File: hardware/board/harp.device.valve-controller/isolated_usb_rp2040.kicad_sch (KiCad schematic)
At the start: 49 parts, among them J2 Conn_01x03_Male, J4 AudioJack3, J5 USB_C_Receptacle_USB2.0, U2 TPD2EUSB30, U3 ADUM4160, U4 RP2040, U5 W25Q16JVUXIQ, X1 ECS-TXO-2016

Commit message: route pcb
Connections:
- net EXT_TRIG0 renamed GPIO0
- net EXT_TRIG1 renamed GPIO1
- net EXT_TRIG2 renamed GPIO2
- net EXT_TRIG3 renamed GPIO3
- net POKE_IN0 renamed GPIO4
- net POKE_IN1 renamed GPIO5
- net POKE_IN2 renamed GPIO6
- net POKE_IN3 renamed GPIO7
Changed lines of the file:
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@@
 		)
 	)
-	(hierarchical_label "EXT_TRIG1"
+	(hierarchical_label "GPIO1"
 		(shape input)
 		(at 227.33 133.35 0)
@@
 		)
 	)
-	(hierarchical_label "POKE_IN0"
+	(hierarchical_label "GPIO4"
 		(shape input)
 		(at 227.33 143.51 0)
@@
 		)
 	)
-	(hierarchical_label "EXT_TRIG2"
+	(hierarchical_label "GPIO2"
 		(shape input)
 		(at 227.33 135.89 0)
@@
 		)
 	)
-	(hierarchical_label "POKE_IN1"
+	(hierarchical_label "GPIO5"
 		(shape input)
 		(at 227.33 146.05 0)
@@
 		)
 	)
-	(hierarchical_label "EXT_TRIG3"
+	(hierarchical_label "GPIO3"
 		(shape input)
 		(at 227.33 138.43 0)
@@
 		)
 	)
-	(hierarchical_label "POKE_IN2"
+	(hierarchical_label "GPIO6"
 		(shape input)
 		(at 227.33 148.59 0)
@@
 		)
 	)
-	(hierarchical_label "EXT_TRIG0"
+	(hierarchical_label "GPIO0"
 		(shape input)
 		(at 227.33 130.81 0)
@@
 		)
 	)
-	(hierarchical_label "POKE_IN3"
+	(hierarchical_label "GPIO7"
 		(shape input)
 		(at 227.33 151.13 0)

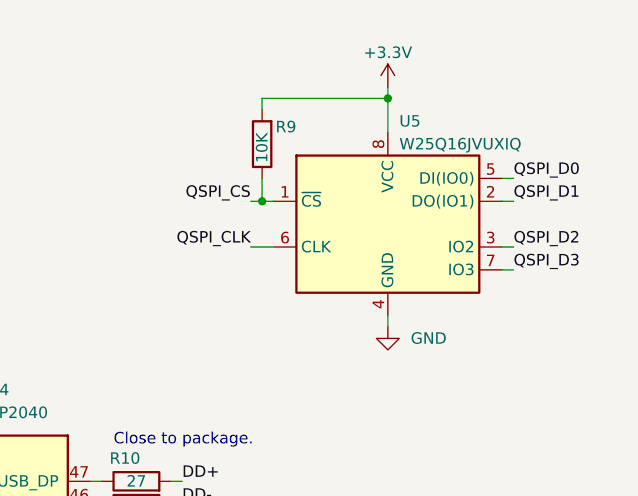
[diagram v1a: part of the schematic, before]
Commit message: update pcb power supply
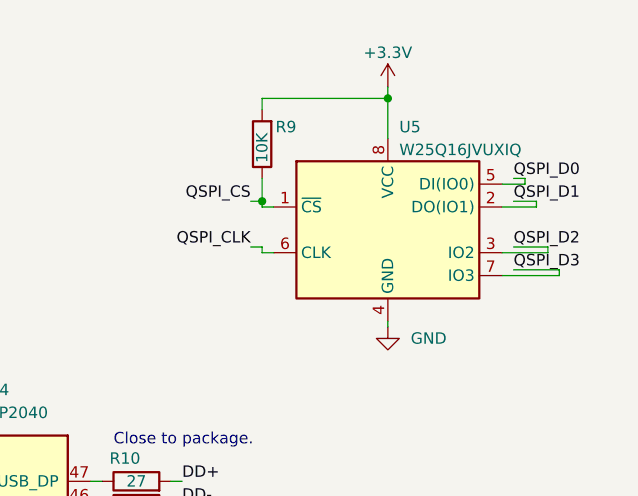
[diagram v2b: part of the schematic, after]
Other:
- moved on the sheet: U5
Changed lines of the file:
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@@
 	(wire
 		(pts
+			(xy 273.05 31.115) (xy 271.78 31.115)
+		)
+		(stroke
+			(width 0)
+			(type default)
+		)
+	)
+	(wire
+		(pts
 			(xy 106.68 27.94) (xy 106.68 31.75)
 		)
@@
 	(wire
 		(pts
-			(xy 257.81 22.225) (xy 257.81 26.035)
+			(xy 257.81 22.225) (xy 257.81 26.67)
 		)
 		(stroke
@@
 	(wire
 		(pts
-			(xy 270.51 38.735) (xy 271.78 38.735)
+			(xy 270.51 39.37) (xy 275.59 39.37)
 		)
 		(stroke
@@
 	(wire
 		(pts
+			(xy 275.59 39.37) (xy 275.59 38.735)
+		)
+		(stroke
+			(width 0)
+			(type default)
+		)
+	)
+	(wire
+		(pts
 			(xy 66.675 38.735) (xy 66.675 53.975)
 		)
@@
 	(wire
 		(pts
+			(xy 274.32 33.655) (xy 271.78 33.655)
+		)
+		(stroke
+			(width 0)
+			(type default)
+		)
+	)
+	(wire
+		(pts
 			(xy 242.57 33.655) (xy 243.84 33.655)
 		)
@@
 	(wire
 		(pts
+			(xy 275.59 38.735) (xy 271.78 38.735)
+		)
+		(stroke
+			(width 0)
+			(type default)
+		)
+	)
+	(wire
+		(pts
 			(xy 42.545 45.085) (xy 41.275 45.085)
 		)
@@
 	(wire
 		(pts
-			(xy 243.84 33.655) (xy 245.11 33.655)
+			(xy 243.84 34.29) (xy 245.11 34.29)
 		)
 		(stroke
@@
 	(wire
 		(pts
+			(xy 276.86 41.275) (xy 271.78 41.275)
+		)
+		(stroke
+			(width 0)
+			(type default)
+		)
+	)
+	(wire
+		(pts
 			(xy 70.485 18.415) (xy 70.485 19.685)
 		)
@@
 	(wire
 		(pts
+			(xy 276.86 41.91) (xy 276.86 41.275)
+		)
+		(stroke
+			(width 0)
+			(type default)
+		)
+	)
+	(wire
+		(pts
 			(xy 180.34 55.88) (xy 175.26 55.88)
 		)
@@
 	(wire
 		(pts
+			(xy 274.32 34.29) (xy 274.32 33.655)
+		)
+		(stroke
+			(width 0)
+			(type default)
+		)
+	)
+	(wire
+		(pts
 			(xy 50.8 180.975) (xy 50.8 179.705)
 		)
@@
 	(wire
 		(pts
-			(xy 257.81 46.355) (xy 257.81 47.625)
+			(xy 257.81 46.99) (xy 257.81 47.625)
 		)
 		(stroke
@@
 	(wire
 		(pts
+			(xy 273.05 31.75) (xy 273.05 31.115)
+		)
+		(stroke
+			(width 0)
+			(type default)
+		)
+	)
+	(wire
+		(pts
 			(xy 224.79 102.87) (xy 227.33 102.87)
 		)
@@
 	(wire
 		(pts
+			(xy 243.84 39.37) (xy 243.84 38.735)
+		)
+		(stroke
+			(width 0)
+			(type default)
+		)
+	)
+	(wire
+		(pts
 			(xy 118.11 22.86) (xy 118.11 26.67)
 		)
@@
 	(wire
 		(pts
+			(xy 243.84 38.735) (xy 242.57 38.735)
+		)
+		(stroke
+			(width 0)
+			(type default)
+		)
+	)
+	(wire
+		(pts
 			(xy 160.02 110.49) (xy 161.29 110.49)
 		)
@@
 	(wire
 		(pts
-			(xy 270.51 33.655) (xy 271.78 33.655)
+			(xy 270.51 34.29) (xy 274.32 34.29)
 		)
 		(stroke
@@
 	(wire
 		(pts
-			(xy 270.51 31.115) (xy 271.78 31.115)
+			(xy 270.51 31.75) (xy 273.05 31.75)
 		)
 		(stroke
@@
 	(wire
 		(pts
+			(xy 243.84 34.29) (xy 243.84 33.655)
+		)
+		(stroke
+			(width 0)
+			(type default)
+		)
+	)
+	(wire
+		(pts
 			(xy 42.545 43.815) (xy 43.815 43.815)
 		)
@@
 	(wire
 		(pts
-			(xy 242.57 38.735) (xy 245.11 38.735)
+			(xy 243.84 39.37) (xy 245.11 39.37)
 		)
 		(stroke
@@
 	(wire
 		(pts
-			(xy 270.51 41.275) (xy 271.78 41.275)
+			(xy 270.51 41.91) (xy 276.86 41.91)
 		)
 		(stroke
@@
 	(symbol
 		(lib_id "Memory_Flash:W25Q128JVS")
-		(at 257.81 36.195 0)
+		(at 257.81 36.83 0)
 		(unit 1)
 		(exclude_from_sim no)
@@
 		(dnp no)
 		(property "Reference" "U5"
-			(at 259.08 24.765 0)
+			(at 259.08 25.4 0)
 			(effects
 				(font
@@
 		)
 		(property "Value" "W25Q16JVUXIQ"
-			(at 259.08 27.305 0)
+			(at 259.08 27.94 0)
 			(effects
 				(font
@@
 		)
 		(property "Footprint" "kicad_component_library:Winbond-8USON-2x3mm"
-			(at 257.81 36.195 0)
+			(at 257.81 36.83 0)
 			(effects
 				(font
@@
 		)
 		(property "Datasheet" "https://www.winbond.com/resource-files/w25q16jv%20spi%20revh%2004082019%20plus.pdf"
-			(at 257.81 36.195 0)
+			(at 257.81 36.83 0)
 			(effects
 				(font
@@
 		)
 		(property "Description" ""
-			(at 257.81 36.195 0)
+			(at 257.81 36.83 0)
 			(effects
 				(font
@@
 		)
 		(property "Link" "https://www.digikey.com/en/products/detail/winbond-electronics/W25Q16JVUXIQ-TR/15182017"
-			(at 257.81 36.195 0)
+			(at 257.81 36.83 0)
 			(effects
 				(font
@@
 		)
 		(property "Manufacturer" "Winbond Electronics"
-			(at 257.81 36.195 0)
+			(at 257.81 36.83 0)
 			(effects
 				(font
@@
 		)
 		(property "Manufacturer Number" "W25Q16JVUXIQ TR"
-			(at 257.81 36.195 0)
+			(at 257.81 36.83 0)
 			(effects
 				(font
@@
 		)
 		(property "PCBWay Link" "https://www.pcbway.com/components"
-			(at 257.81 36.195 0)
+			(at 257.81 36.83 0)
 			(effects
 				(font

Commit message: prep hw initial release
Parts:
- added J21: Conn_01x03_Male, Connector_PinHeader_2.54mm:PinHeader_1x03_P2.54mm_Vertical, symbol Connector:Conn_01x03_Male
- C1, C12, C13, C14, C15, C16, C17, C18, C19, C2, C3, C37, C5, C6, C7: Link https://www.digikey.com/en/products/detail/walsin-technolog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 -> https://www.digikey.com/en/products/detail/murata-electroni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; Manufacturer Walson Technology Corporation -> Murata Electronics; Manufacturer Number 0402B104K160CT -> GRM155R71H104KE14D; Rated Voltage 16V -> 50V
- C11: Alternate CL21B106KOQNNNE -> (none); Link https://www.digikey.com/en/products/detail/murata-electroni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 -> https://www.digikey.com/en/products/detail/cal-chip-electro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; Manufacturer Murata Electronics -> Cal-Chip Electronics, Inc.; Manufacturer Number GRM21BZ71E106KE15L -> GMC21X7R106K25NT; Rated Voltage 25V -> (none); Temperature Coefficient X7R -> (none)
- D3, D4: Link https://www.digikey.com/en/products/detail/onsemi/ESD7571N2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 -> https://www.digikey.com/en/products/detail/nexperia-usa-inc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; Manufacturer onsemi -> Nexperia USA Inc.; Manufacturer Number ESD7571N2T5G -> PESD5V0F1BLD,315
- R9: Link https://www.digikey.com/en/products/detail/koa-speer-electr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 -> https://www.digikey.com/en/products/detail/stackpole-electr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; Manufacturer KOA Speer Electronics, Inc. -> Stackpole Electronics Inc; Manufacturer Number SG73P1EWTTP1002F -> RNCF0402BTE10K0
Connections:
- net +3.3V: now also R9.1; no longer R9.2
- net GND: now also J21.3 (Pin_3)
- net QSPI_CS: now also R9.2; no longer R9.1
- net at U4.24 (SWCLK): now also J21.1 (Pin_1)
- net at U4.25 (SWD): now also J21.2 (Pin_2)
- no-connect marks 9 -> 7
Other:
- note added: "SWD"
- moved on the sheet: C12, C13, C14, C15, C16, C17, C18, C19, U5
